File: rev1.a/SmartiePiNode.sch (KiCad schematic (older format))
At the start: 63 parts, among them CN1 USBMICROb, CN2 SWD, CN3 SX1238_TRX_HEADER, CN4 VIN, P1 SENSOR_GPIO, SW1 SW_PUSH, U1 ISL91127IR, U2 STM32L052_LQFP48, X1 abm10, X2 ABS25-32.768KHZ-6-T

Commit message: finished routing of rev1.a
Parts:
- renumbered P1 to CN5
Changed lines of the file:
@@
 $EndComp
 $Comp
-L GND #PWR11
+L GND #PWR01
 U 1 1 5B041A53
 P 3720 7315
-F 0 "#PWR11" H 3720 7065 50  0001 C CNN
+F 0 "#PWR01" H 3720 7065 50  0001 C CNN
 F 1 "GND" H 3725 7142 50  0000 C CNN
 F 2 "" H 3720 7315 50  0001 C CNN
@@
 $EndComp
 $Comp
-L GND #PWR16
+L GND #PWR02
 U 1 1 5B041F18
 P 4975 6485
-F 0 "#PWR16" H 4975 6235 50  0001 C CNN
+F 0 "#PWR02" H 4975 6235 50  0001 C CNN
 F 1 "GND" H 4980 6312 50  0000 C CNN
 F 2 "" H 4975 6485 50  0001 C CNN
@@
 $EndComp
 $Comp
-L GND #PWR17
+L GND #PWR03
 U 1 1 5B04234F
 P 5255 6485
-F 0 "#PWR17" H 5255 6235 50  0001 C CNN
+F 0 "#PWR03" H 5255 6235 50  0001 C CNN
 F 1 "GND" H 5260 6312 50  0000 C CNN
 F 2 "" H 5255 6485 50  0001 C CNN
@@
 $EndComp
 $Comp
-L GND #PWR19
+L GND #PWR04
 U 1 1 5B0423C8
 P 5530 6485
-F 0 "#PWR19" H 5530 6235 50  0001 C CNN
+F 0 "#PWR04" H 5530 6235 50  0001 C CNN
 F 1 "GND" H 5535 6312 50  0000 C CNN
 F 2 "" H 5530 6485 50  0001 C CNN
@@
 $EndComp
 $Comp
-L GND #PWR7
+L GND #PWR05
 U 1 1 5B04306E
 P 2340 6485
-F 0 "#PWR7" H 2340 6235 50  0001 C CNN
+F 0 "#PWR05" H 2340 6235 50  0001 C CNN
 F 1 "GND" H 2345 6312 50  0000 C CNN
 F 2 "" H 2340 6485 50  0001 C CNN
@@
 $EndComp
 $Comp
-L GND #PWR5
+L GND #PWR06
 U 1 1 5B04307C
 P 2060 6485
-F 0 "#PWR5" H 2060 6235 50  0001 C CNN
+F 0 "#PWR06" H 2060 6235 50  0001 C CNN
 F 1 "GND" H 2065 6312 50  0000 C CNN
 F 2 "" H 2060 6485 50  0001 C CNN
@@
 $EndComp
 $Comp
-L GND #PWR4
+L GND #PWR07
 U 1 1 5B04308A
 P 1785 6485
-F 0 "#PWR4" H 1785 6235 50  0001 C CNN
+F 0 "#PWR07" H 1785 6235 50  0001 C CNN
 F 1 "GND" H 1790 6312 50  0000 C CNN
 F 2 "" H 1785 6485 50  0001 C CNN
@@
 $EndComp
 $Comp
-L GND #PWR8
+L GND #PWR08
 U 1 1 5B043F5D
 P 2705 7280
-F 0 "#PWR8" H 2705 7030 50  0001 C CNN
+F 0 "#PWR08" H 2705 7030 50  0001 C CNN
 F 1 "GND" H 2710 7107 50  0000 C CNN
 F 2 "" H 2705 7280 50  0001 C CNN
@@
 $EndComp
 $Comp
-L GND #PWR13
+L GND #PWR09
 U 1 1 5B044D4C
 P 4485 7315
-F 0 "#PWR13" H 4485 7065 50  0001 C CNN
+F 0 "#PWR09" H 4485 7065 50  0001 C CNN
 F 1 "GND" H 4490 7142 50  0000 C CNN
 F 2 "" H 4485 7315 50  0001 C CNN
@@
 $EndComp
 $Comp
-L GND #PWR26
+L GND #PWR010
 U 1 1 5B06F6EF
 P 9930 3790
-F 0 "#PWR26" H 9930 3540 50  0001 C CNN
+F 0 "#PWR010" H 9930 3540 50  0001 C CNN
 F 1 "GND" H 9935 3617 50  0000 C CNN
 F 2 "" H 9930 3790 50  0001 C CNN
@@
 $EndComp
 $Comp
-L GND #PWR23
+L GND #PWR011
 U 1 1 5B0753BB
 P 6760 3380
-F 0 "#PWR23" H 6760 3130 50  0001 C CNN
+F 0 "#PWR011" H 6760 3130 50  0001 C CNN
 F 1 "GND" H 6765 3207 50  0000 C CNN
 F 2 "" H 6760 3380 50  0001 C CNN
@@
 $EndComp
 $Comp
-L GND #PWR3
+L GND #PWR012
 U 1 1 5B081C3A
 P 1715 4725
-F 0 "#PWR3" H 1715 4475 50  0001 C CNN
+F 0 "#PWR012" H 1715 4475 50  0001 C CNN
 F 1 "GND" H 1720 4552 50  0000 C CNN
 F 2 "" H 1715 4725 50  0001 C CNN
@@
 $EndComp
 $Comp
-L GND #PWR21
+L GND #PWR013
 U 1 1 5B082DC4
 P 5880 3240
-F 0 "#PWR21" H 5880 2990 50  0001 C CNN
+F 0 "#PWR013" H 5880 2990 50  0001 C CNN
 F 1 "GND" H 5885 3067 50  0000 C CNN
 F 2 "" H 5880 3240 50  0001 C CNN
@@
 Connection ~ 10575 2935
 $Comp
-L GND #PWR28
+L GND #PWR014
 U 1 1 5B098D9A
 P 11070 2830
-F 0 "#PWR28" H 11070 2580 50  0001 C CNN
+F 0 "#PWR014" H 11070 2580 50  0001 C CNN
 F 1 "GND" H 11075 2657 50  0000 C CNN
 F 2 "" H 11070 2830 50  0001 C CNN
@@
 	2225 1540 2225 1670
 $Comp
-L GND #PWR6
+L GND #PWR015
 U 1 1 5B0A5E1E
 P 2225 1670
-F 0 "#PWR6" H 2225 1420 50  0001 C CNN
+F 0 "#PWR015" H 2225 1420 50  0001 C CNN
 F 1 "GND" H 2230 1497 50  0000 C CNN
 F 2 "" H 2225 1670 50  0001 C CNN
@@
 +3V3
 $Comp
-L GND #PWR9
+L GND #PWR016
 U 1 1 5B0AC996
 P 3070 1200
-F 0 "#PWR9" H 3070 950 50  0001 C CNN
+F 0 "#PWR016" H 3070 950 50  0001 C CNN
 F 1 "GND" H 3075 1027 50  0000 C CNN
 F 2 "" H 3070 1200 50  0001 C CNN
@@
 SPI2_SCK
 $Comp
-L GND #PWR10
+L GND #PWR017
 U 1 1 5B0AE690
 P 3070 1500
-F 0 "#PWR10" H 3070 1250 50  0001 C CNN
+F 0 "#PWR017" H 3070 1250 50  0001 C CNN
 F 1 "GND" H 3075 1327 50  0000 C CNN
 F 2 "" H 3070 1500 50  0001 C CNN
@@
 	4145 2100 4720 2100
 $Comp
-L GND #PWR14
+L GND #PWR018
 U 1 1 5B0AEB87
 P 4720 2100
-F 0 "#PWR14" H 4720 1850 50  0001 C CNN
+F 0 "#PWR018" H 4720 1850 50  0001 C CNN
 F 1 "GND" H 4725 1927 50  0000 C CNN
 F 2 "" H 4720 2100 50  0001 C CNN
@@
 	1625 3160 1695 3160
 $Comp
-L GND #PWR2
+L GND #PWR019
 U 1 1 5B0B10C1
 P 1695 3160
-F 0 "#PWR2" H 1695 2910 50  0001 C CNN
+F 0 "#PWR019" H 1695 2910 50  0001 C CNN
 F 1 "GND" H 1700 2987 50  0000 C CNN
 F 2 "" H 1695 3160 50  0001 C CNN
@@
 NRST
 $Comp
-L GND #PWR12
+L GND #PWR020
 U 1 1 5B0B8F14
 P 4200 3080
-F 0 "#PWR12" H 4200 2830 50  0001 C CNN
+F 0 "#PWR020" H 4200 2830 50  0001 C CNN
 F 1 "GND" H 4205 2907 50  0000 C CNN
 F 2 "" H 4200 3080 50  0001 C CNN
@@
 $EndComp
 $Comp
-L GND #PWR24
+L GND #PWR021
 U 1 1 5B0C38AE
 P 8160 5860
-F 0 "#PWR24" H 8160 5610 50  0001 C CNN
+F 0 "#PWR021" H 8160 5610 50  0001 C CNN
 F 1 "GND" H 8165 5687 50  0000 C CNN
 F 2 "" H 8160 5860 50  0001 C CNN
@@
 Connection ~ 6235 2750
 $Comp
-L GND #PWR22
+L GND #PWR022
 U 1 1 5B1AE42D
 P 6235 2785
-F 0 "#PWR22" H 6235 2535 50  0001 C CNN
+F 0 "#PWR022" H 6235 2535 50  0001 C CNN
 F 1 "GND" H 6315 2770 50  0000 C CNN
 F 2 "" H 6235 2785 50  0001 C CNN
@@
 	4855 4565 4855 5170
 $Comp
-L GND #PWR15
+L GND #PWR023
 U 1 1 5B1D46F6
 P 4855 5170
-F 0 "#PWR15" H 4855 4920 50  0001 C CNN
+F 0 "#PWR023" H 4855 4920 50  0001 C CNN
 F 1 "GND" H 4860 4997 50  0000 C CNN
 F 2 "" H 4855 5170 50  0001 C CNN
@@
 	1290 5510 1290 5615
 $Comp
-L GND #PWR1
+L GND #PWR024
 U 1 1 5B2467F2
 P 1290 5615
-F 0 "#PWR1" H 1290 5365 50  0001 C CNN
+F 0 "#PWR024" H 1290 5365 50  0001 C CNN
 F 1 "GND" H 1295 5442 50  0000 C CNN
 F 2 "" H 1290 5615 50  0001 C CNN
@@
 	5270 1400 5270 1525
 $Comp
-L GND #PWR18
+L GND #PWR025
 U 1 1 5B27DE3A
 P 5270 1525
-F 0 "#PWR18" H 5270 1275 50  0001 C CNN
+F 0 "#PWR025" H 5270 1275 50  0001 C CNN
 F 1 "GND" H 5275 1352 50  0000 C CNN
 F 2 "" H 5270 1525 50  0001 C CNN
@@
 	5740 1345 5740 1395
 $Comp
-L GND #PWR20
+L GND #PWR026
 U 1 1 5B2802E4
 P 5740 1395
-F 0 "#PWR20" H 5740 1145 50  0001 C CNN
+F 0 "#PWR026" H 5740 1145 50  0001 C CNN
 F 1 "GND" H 5745 1222 50  0000 C CNN
 F 2 "" H 5740 1395 50  0001 C CNN
@@
 	6515 1290 7375 1290
 $Comp
-L CONN_02X08 P1
+L CONN_02X08 CN5
 U 1 1 5B364EB8
 P 10240 5170
-F 0 "P1" H 10175 4730 50  0000 C CNN
+F 0 "CN5" H 10175 4730 50  0000 C CNN
 F 1 "SENSOR_GPIO" H 10240 5644 50  0000 C CNN
 F 2 "Pin_Headers:Pin_Header_Straight_2x08" H 10240 3970 50  0001 C CNN
@@
 	9880 5520 9880 5600
 $Comp
-L GND #PWR25
+L GND #PWR027
 U 1 1 5B3670FD
 P 9880 5600
-F 0 "#PWR25" H 9880 5350 50  0001 C CNN
+F 0 "#PWR027" H 9880 5350 50  0001 C CNN
 F 1 "GND" H 9885 5427 50  0000 C CNN
 F 2 "" H 9880 5600 50  0001 C CNN
@@
 +3V3
 $Comp
-L GND #PWR27
+L GND #PWR028
 U 1 1 5B379033
 P 11030 4820
-F 0 "#PWR27" H 11030 4570 50  0001 C CNN
+F 0 "#PWR028" H 11030 4570 50  0001 C CNN
 F 1 "GND" V 11105 4840 50  0000 R CNN
 F 2 "" H 11030 4820 50  0001 C CNN

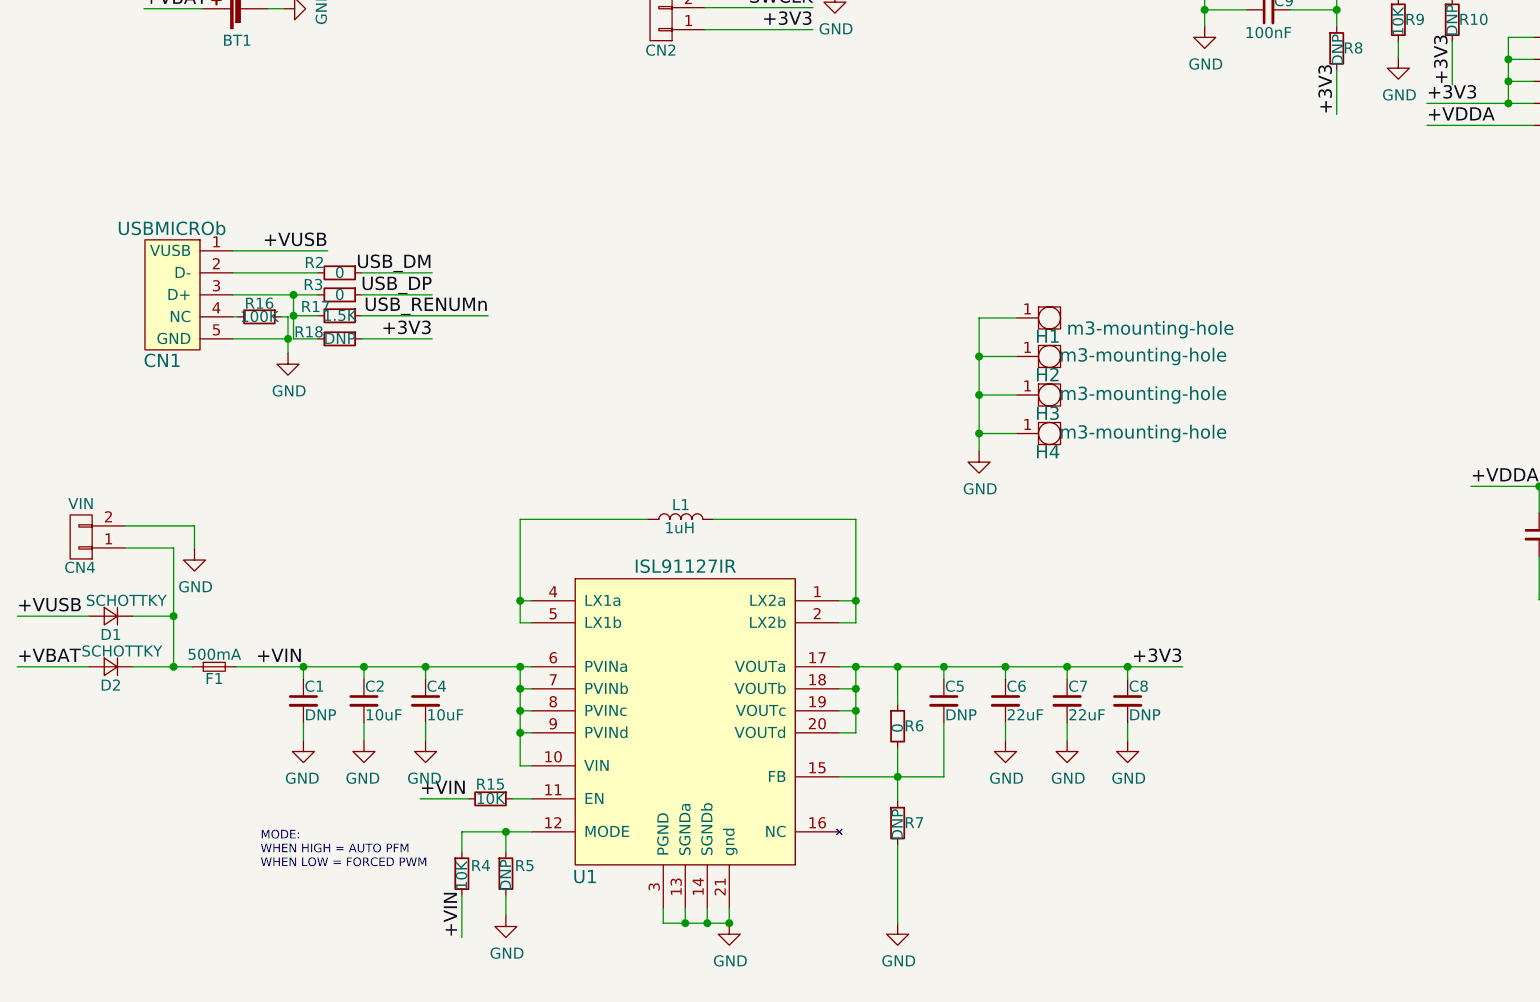
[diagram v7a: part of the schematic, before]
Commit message: added optional power switch
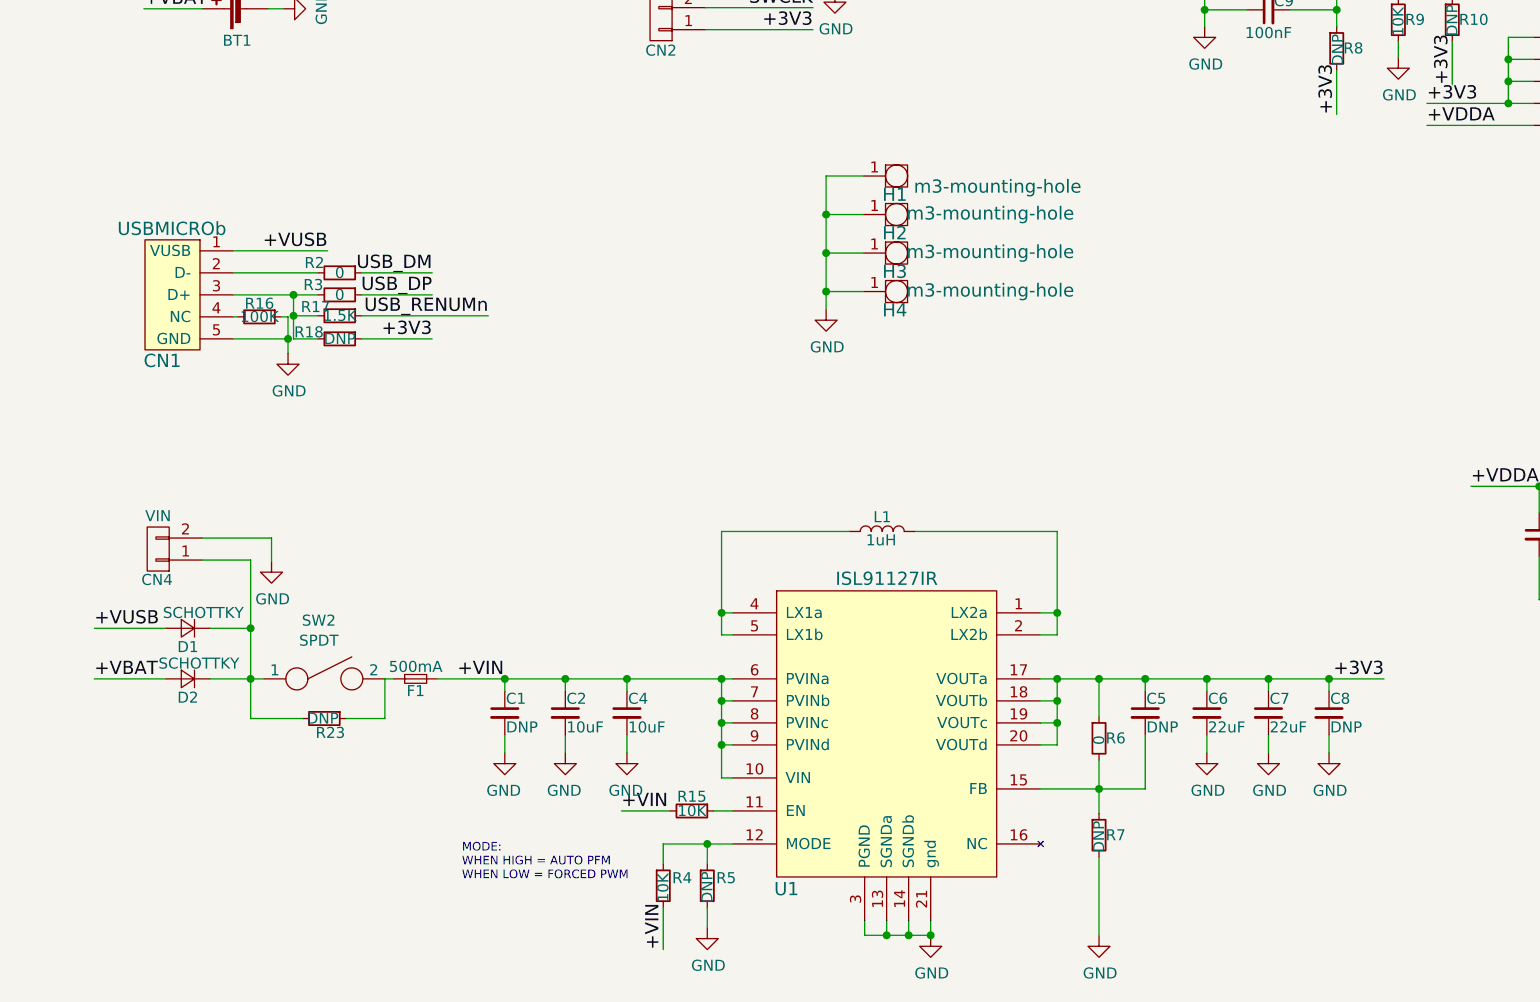
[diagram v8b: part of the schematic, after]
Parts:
- added R23: DNP, Resistors_SMD:R_0603, symbol R_Small
- added SW2: SPDT, copal-cl-sb-12a:copal-cl-sb-12a, symbol SPDT
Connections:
- net at CN4.1 (P1), D1.1 (K), D2.1 (K): now also R23.2, SW2.1; no longer F1.1
- new net: F1.1, R23.1, SW2.2
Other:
- moved on the sheet: C1, C2, C4, C5, C6, C7, C8, CN4, D1, D2, F1, H1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
